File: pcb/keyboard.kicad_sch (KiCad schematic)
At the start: 58 parts, among them J1 TRRS, SW11 11, SW12 12, SW13 13, SW14 14, SW15 15, SW16 16, SW17 17, SW18 18, SW19 19, SW21 21, SW22 22, SW23 23, SW24 24, SW25 25, SW26 26, SW27 27, SW28 28, SW29 29, SW31 31, SW32 32, SW33 33, SW34 34, SW35 35, SW36 36, SW37 37, SW38 38, SW39 39, SW41 41, SW42 42, SW43 43, SW45 45, SW46 46, SW47 47, SW48 48, SW49 49, U1 EliteC

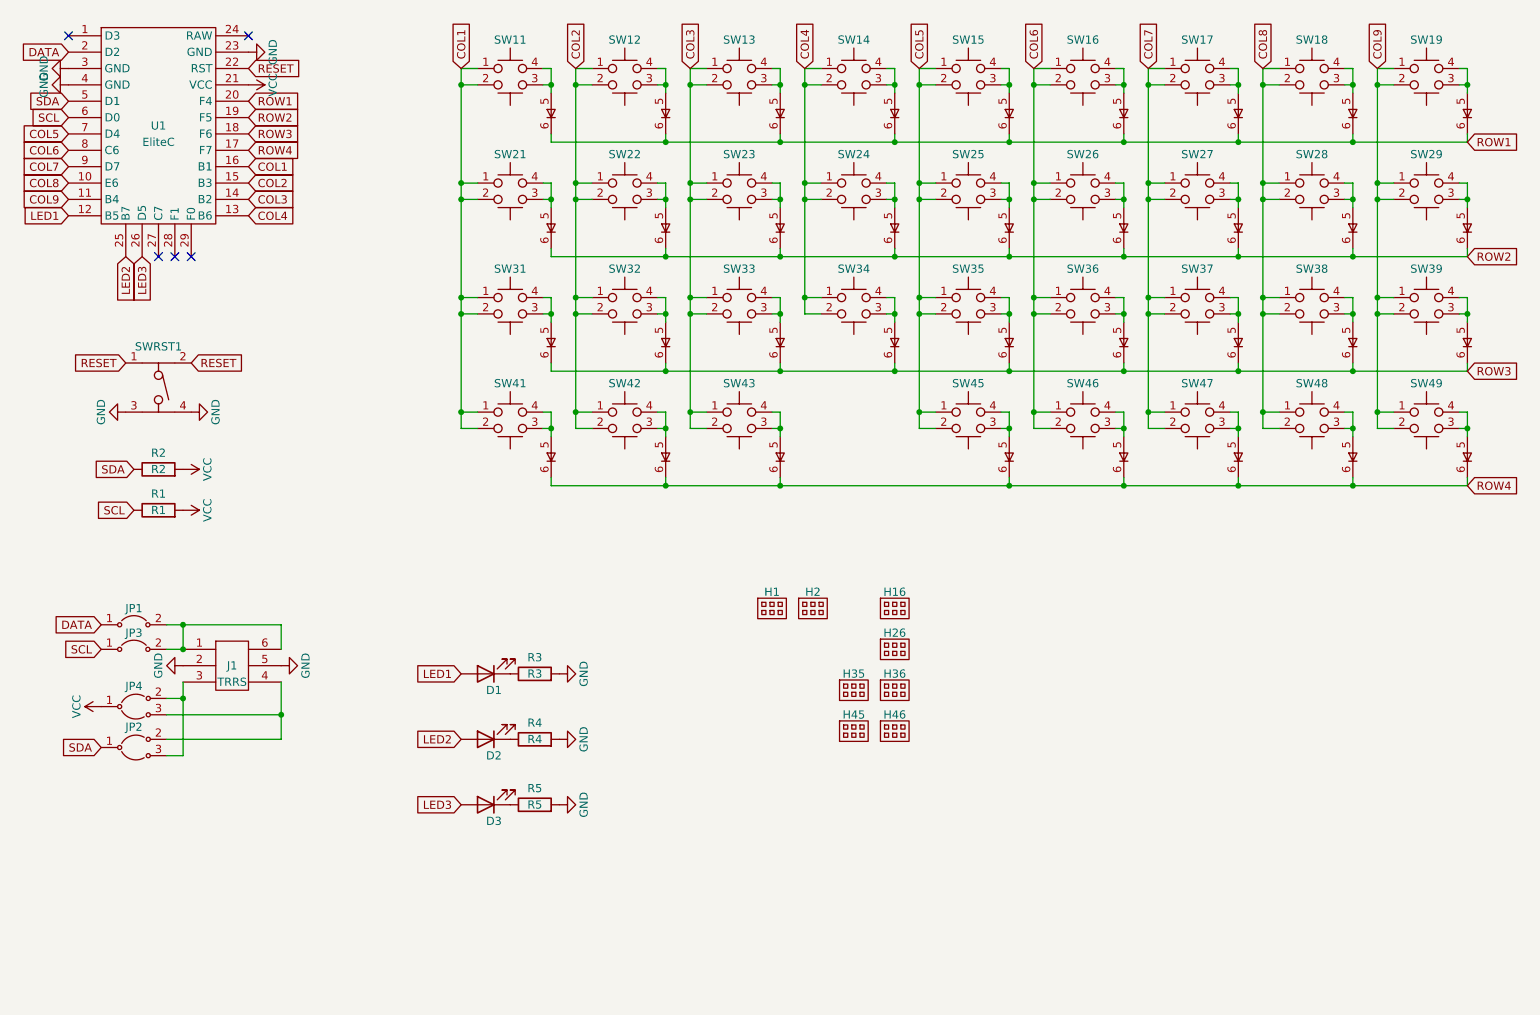
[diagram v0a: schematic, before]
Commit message: rework footprints with 3d models
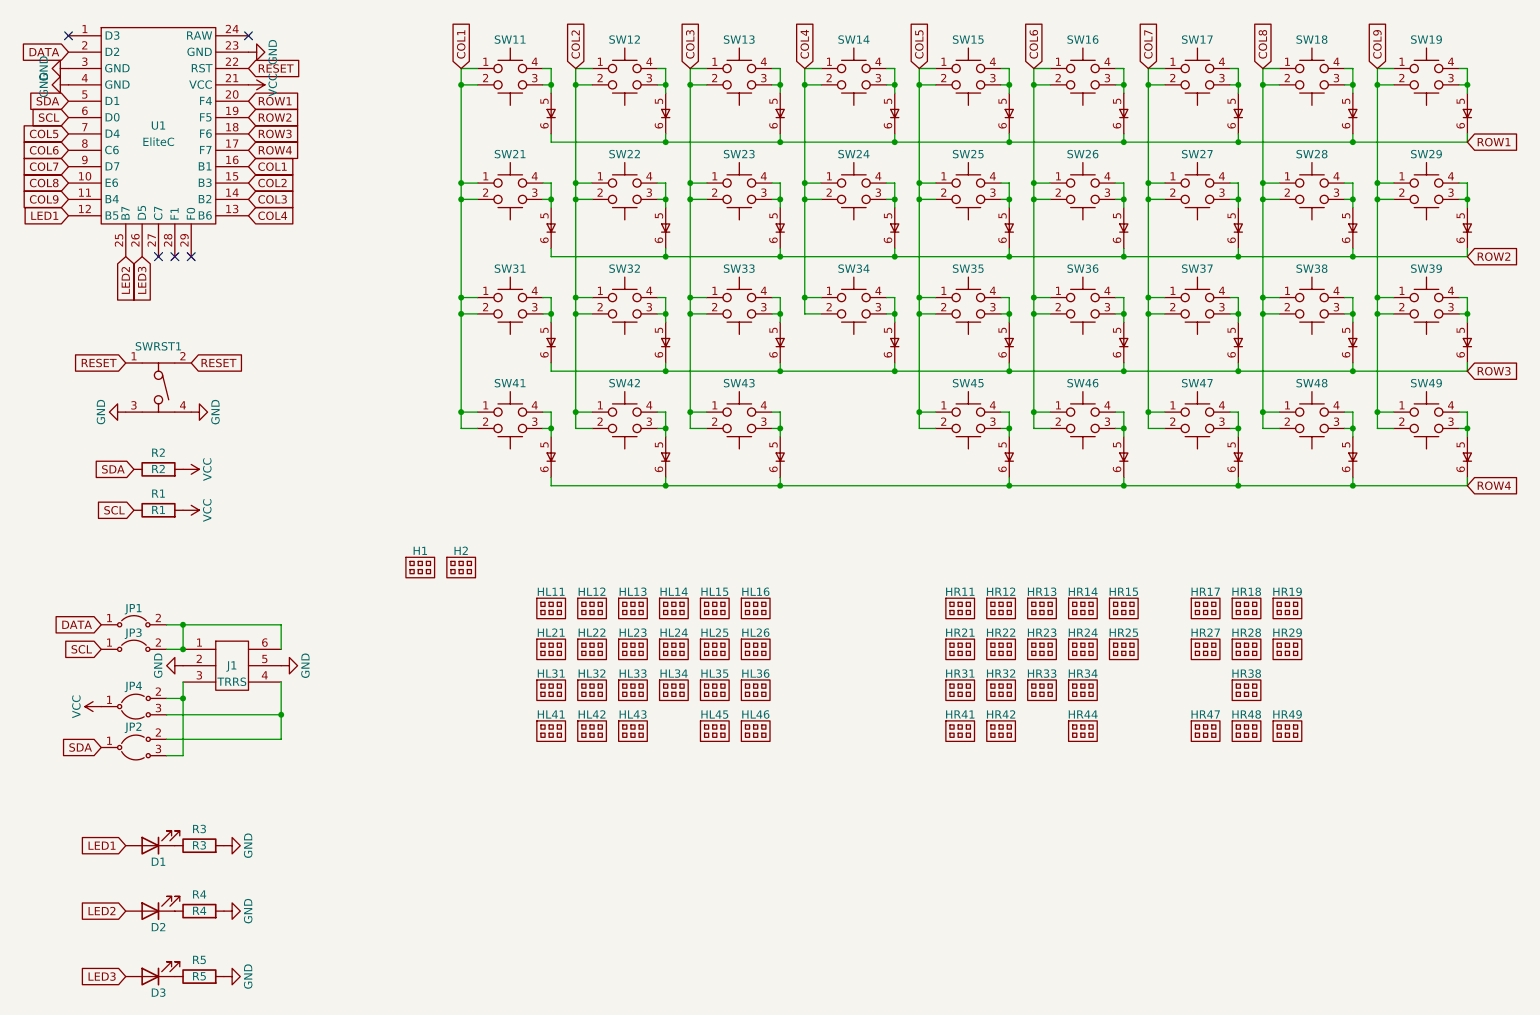
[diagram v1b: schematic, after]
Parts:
- removed H16: H16, Keyboard:SwitchDoubleNo3D, symbol Keyboard:Plate
- removed H26: H26, Keyboard:SwitchDoubleNo3D, symbol Keyboard:Plate
- removed H35: H35, Keyboard:SwitchDoubleNo3D, symbol Keyboard:Plate
- removed H36: H36, Keyboard:SwitchDoubleNo3D, symbol Keyboard:Plate
- removed H45: H45, Keyboard:SwitchDoubleNo3D, symbol Keyboard:Plate
- removed H46: H46, Keyboard:SwitchDoubleNo3D, symbol Keyboard:Plate
- added HL11, HL12, HL13, HL14, HL15, HL21, HL22, HL23, HL24, HL25, HL31, HL32, HL33, HL34, HL41, HL42, HL43: ~, Keyboard:Switch3DLeft, symbol Keyboard:Plate
- added HL16, HL26, HL35, HL36, HL45, HL46: ~, Keyboard:SwitchDoubleLeft, symbol Keyboard:Plate
- added HR11, HR12, HR13, HR14, HR15, HR17, HR18, HR19, HR21, HR22, HR23, HR24, HR25, HR27, HR28, HR29, HR31, HR32, HR33, HR34, HR38, HR41, HR42, HR44, HR47, HR48, HR49: ~, Keyboard:Switch3DRight, symbol Keyboard:Plate
- SW16, SW26, SW35, SW36, SW45, SW46: footprint Keyboard:SwitchDouble -> Keyboard:SwitchDoubleRight
- SW37, SW39: footprint Keyboard:SwitchNo3D -> Keyboard:Switch
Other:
- moved on the sheet: D1, D2, D3, H1, H2, R3, R4, R5

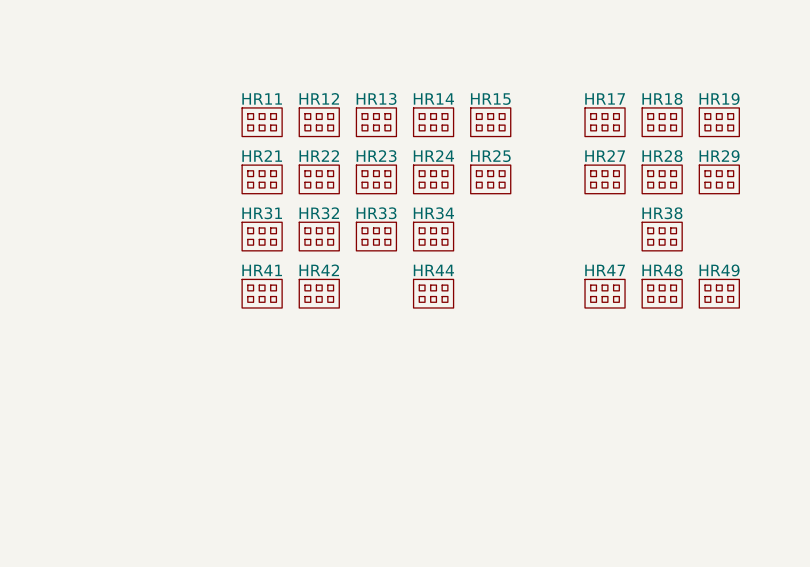
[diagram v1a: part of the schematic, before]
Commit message: move 3d footprints into position
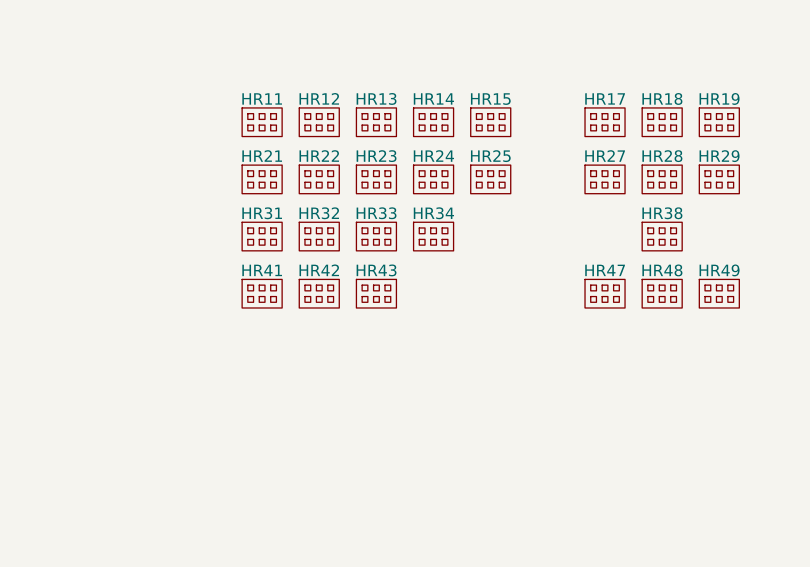
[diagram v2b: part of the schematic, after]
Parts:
- renumbered HR44 to HR43
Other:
- moved on the sheet: HR43
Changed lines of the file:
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@@
     )
   )
-  (symbol (lib_id "Keyboard:Plate") (at 199.39 142.24 0) (unit 1)
+  (symbol (lib_id "Keyboard:Plate") (at 193.04 142.24 0) (unit 1)
     (in_bom yes) (on_board yes) (dnp no) (fields_autoplaced)
-    (property "Reference" "HR44" (at 199.39 139.7 0) (do_not_autoplace)
+    (property "Reference" "HR43" (at 193.04 139.7 0) (do_not_autoplace)
       (effects (font (size 1.27 1.27)))
     )
-    (property "Value" "~" (at 198.4375 141.9225 0) (do_not_autoplace)
+    (property "Value" "~" (at 192.0875 141.9225 0) (do_not_autoplace)
       (effects (font (size 1.27 1.27)) hide)
     )
-    (property "Footprint" "Keyboard:Switch3DRight" (at 198.4375 141.9225 0)
+    (property "Footprint" "Keyboard:Switch3DRight" (at 192.0875 141.9225 0)
       (effects (font (size 1.27 1.27)) hide)
     )
-    (property "Datasheet" "" (at 198.4375 141.9225 0)
+    (property "Datasheet" "" (at 192.0875 141.9225 0)
       (effects (font (size 1.27 1.27)) hide)
     )
@@
       (project "keyboard"
         (path "/7807834d-3d77-4d25-b9d8-d933072c7b84"
-          (reference "HR44") (unit 1)
+          (reference "HR43") (unit 1)
         )
       )

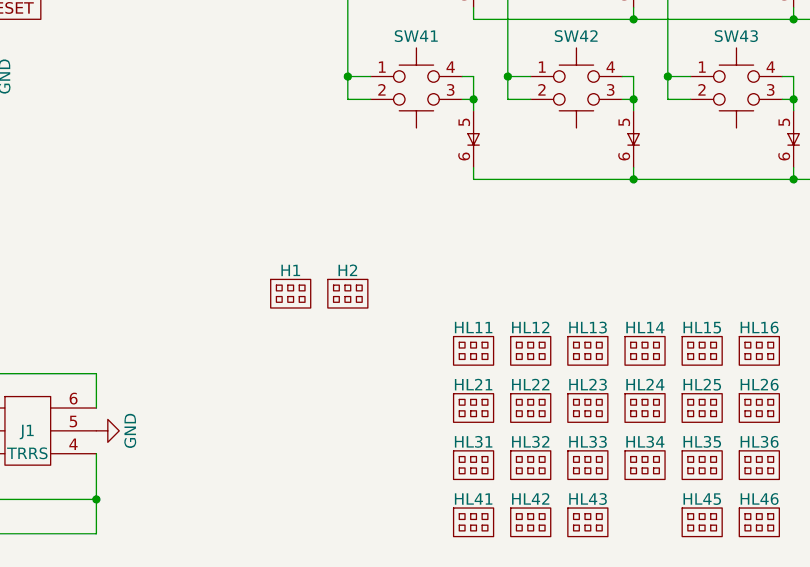
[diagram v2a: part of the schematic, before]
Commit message: add controller-plate
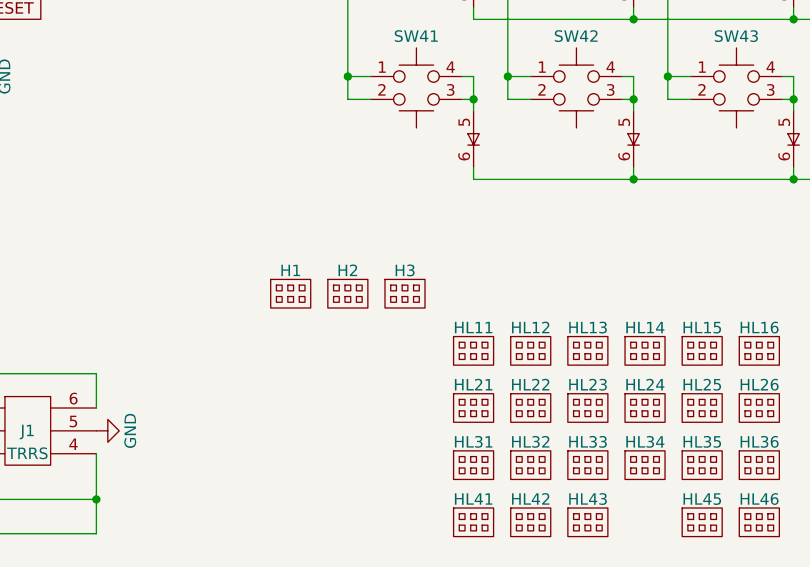
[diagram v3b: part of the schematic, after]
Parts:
- added H3: H2, Keyboard:ControllerPlate, symbol Keyboard:Plate
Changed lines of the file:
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@@
+    )
+  )
+  (symbol (lib_id "Keyboard:Plate") (at 109.22 116.84 0) (unit 1)
+    (in_bom yes) (on_board yes) (dnp no) (fields_autoplaced)
+    (property "Reference" "H3" (at 109.22 114.3 0) (do_not_autoplace)
+      (effects (font (size 1.27 1.27)))
+    )
+    (property "Value" "H2" (at 108.2675 116.5225 0) (do_not_autoplace)
+      (effects (font (size 1.27 1.27)) hide)
+    )
+    (property "Footprint" "Keyboard:ControllerPlate" (at 108.2675 116.5225 0)
+      (effects (font (size 1.27 1.27)) hide)
+    )
+    (property "Datasheet" "" (at 108.2675 116.5225 0)
+      (effects (font (size 1.27 1.27)) hide)
+    )
+    (instances
+      (project "keyboard"
+        (path "/7807834d-3d77-4d25-b9d8-d933072c7b84"
+          (reference "H3") (unit 1)
+        )
+      )
     )
   )
